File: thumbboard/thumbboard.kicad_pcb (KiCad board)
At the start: 2 copper layers, 79.7 x 37 mm, 6 parts, among them J1 Conn_01x05_MountingPin, SW1 SW_Push, SW2 SW_Push, SW3 SW_Push, SW4 SW_Push

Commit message: sdf
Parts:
- removed the REF** at (114.1, 89.2)
- added REF**: NPTH 0.5mm, panelization:NPTH 0.5mm, F.Cu at (137.5, 80.0)
- added REF**: NPTH 0.5mm, panelization:NPTH 0.5mm, F.Cu at (137.5, 79.0)
- added REF**: NPTH 0.5mm, panelization:NPTH 0.5mm, F.Cu at (137.5, 78.0)
- added REF**: NPTH 0.5mm, panelization:NPTH 0.5mm, F.Cu at (128.5, 92.0)
- added REF**: NPTH 0.5mm, panelization:NPTH 0.5mm, F.Cu at (128.5, 90.0)
- added REF**: NPTH 0.5mm, panelization:NPTH 0.5mm, F.Cu at (128.5, 91.0)
- moved SW4 8.06 mm to (169.0, 85.0), turned to -90 degrees
- moved J1 7.07 mm to (145.0, 78.9)
- moved SW1 7.07 mm to (145.0, 85.0)
- moved SW2 7.07 mm to (145.0, 105.5)
- moved SW3 2.24 mm to (121.0, 85.0), turned to 90 degrees
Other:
- board size 79.7 x 37 mm -> 63 x 37 mm

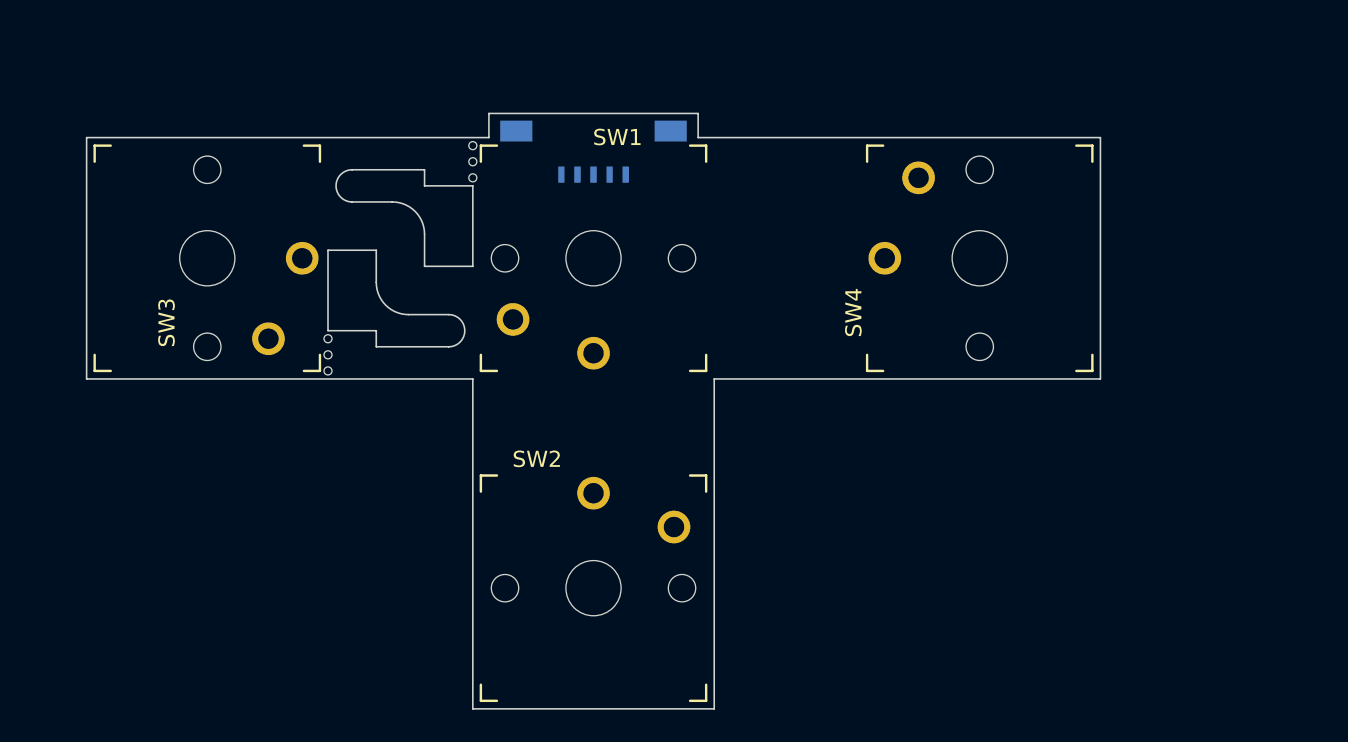
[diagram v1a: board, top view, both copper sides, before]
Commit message: small tweaks, incl thumbboard side springs (and fabrication frame)
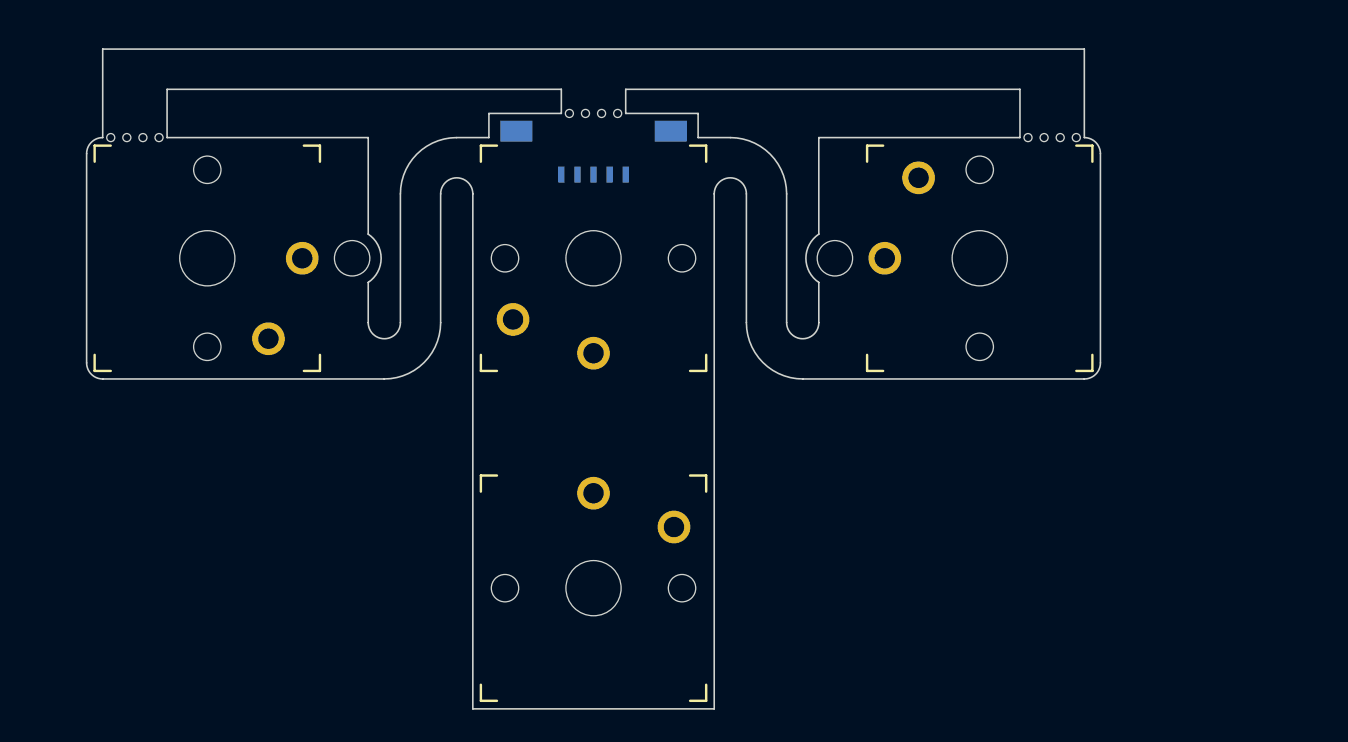
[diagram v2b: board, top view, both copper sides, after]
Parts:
- removed the REF** at (137.5, 80.0)
- removed the REF** at (137.5, 79.0)
- removed the REF** at (137.5, 78.0)
- removed the REF** at (128.5, 92.0)
- removed the REF** at (128.5, 90.0)
- removed the REF** at (128.5, 91.0)
- added REF**: NPTH 0.5mm, panelization:NPTH 0.5mm, F.Cu at (145.5, 76.0)
- added REF**: NPTH 0.5mm, panelization:NPTH 0.5mm, B.Cu at (175.0, 77.5)
- added REF**: NPTH 0.5mm, panelization:NPTH 0.5mm, B.Cu at (174.0, 77.5)
- added REF**: NPTH 0.5mm, panelization:NPTH 0.5mm, B.Cu at (173.0, 77.5)
- added REF**: NPTH 0.5mm, panelization:NPTH 0.5mm, B.Cu at (172.0, 77.5)
- added REF**: NPTH 2.2mm, panelization:NPTH 2.2mm, B.Cu at (160.0, 85.0)
- added REF**: NPTH 0.5mm, panelization:NPTH 0.5mm, F.Cu at (115.0, 77.5)
- added REF**: NPTH 0.5mm, panelization:NPTH 0.5mm, F.Cu at (144.5, 76.0)
- added REF**: NPTH 2.2mm, panelization:NPTH 2.2mm, F.Cu at (130.0, 85.0)
- added REF**: NPTH 0.5mm, panelization:NPTH 0.5mm, F.Cu at (146.5, 76.0)
- added REF**: NPTH 0.5mm, panelization:NPTH 0.5mm, F.Cu at (118.0, 77.5)
- added REF**: NPTH 0.5mm, panelization:NPTH 0.5mm, F.Cu at (116.0, 77.5)
- added REF**: NPTH 0.5mm, panelization:NPTH 0.5mm, F.Cu at (143.5, 76.0)
- added REF**: NPTH 0.5mm, panelization:NPTH 0.5mm, F.Cu at (117.0, 77.5)
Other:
- board size 63 x 37 mm -> 63 x 41 mm

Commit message: layout and cleanups (but J1 still in the wrong spot)
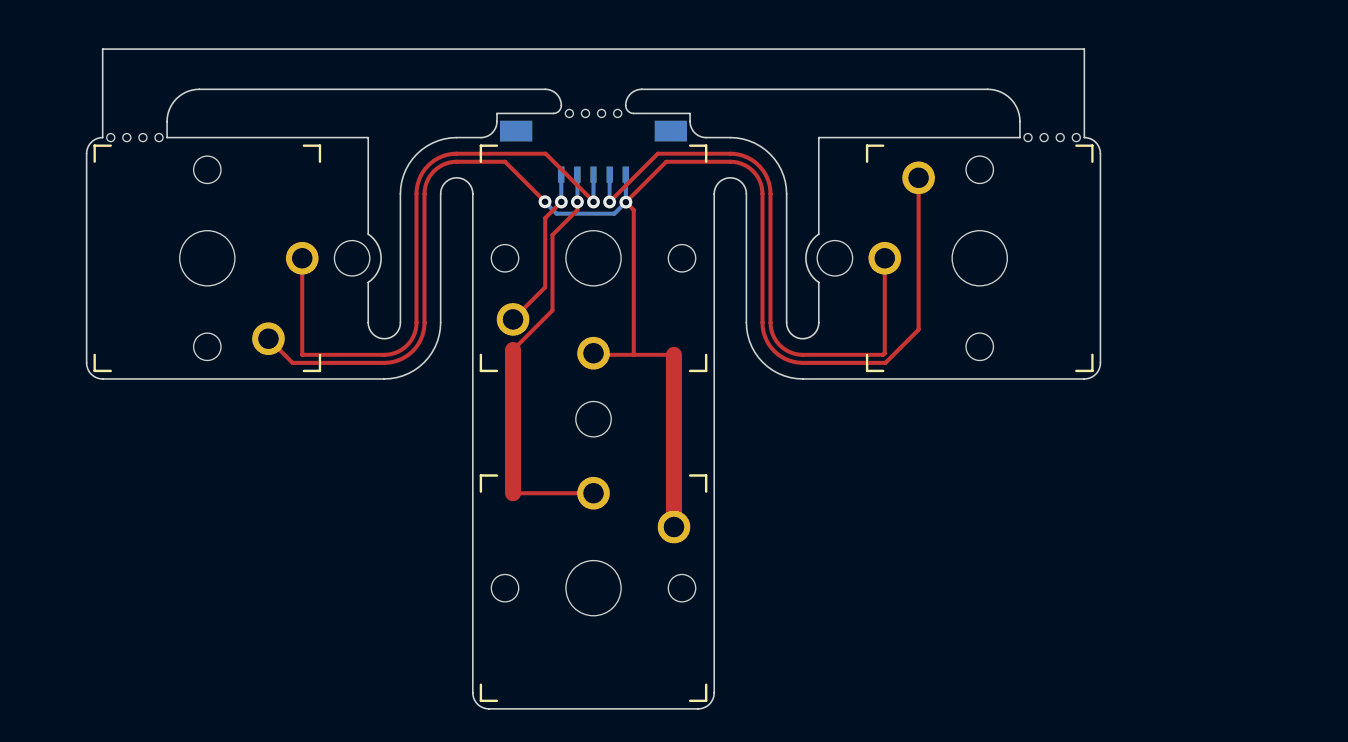
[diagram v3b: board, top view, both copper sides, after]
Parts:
- added REF**: NPTH 2.2mm, panelization:NPTH 2.2mm, F.Cu at (145.0, 95.0)
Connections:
- SW1 pad 1: ROW_A -> COL
- SW1 pad 2: COL -> ROW_A
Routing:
- net COL: track 0.00 -> 102.0 mm, vias 0 -> 2
- net ROW_C: track 0.00 -> 37.4 mm, vias 0 -> 1
- net ROW_D: track 0.00 -> 36.4 mm, vias 0 -> 1
- net ROW_B: track 0.00 -> 26.5 mm, vias 0 -> 1
- net ROW_A: track 0.00 -> 10.2 mm, vias 0 -> 1
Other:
- outline, holes or cut-outs redrawn

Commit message: more tweaks to thumbboard, incl changing pinout
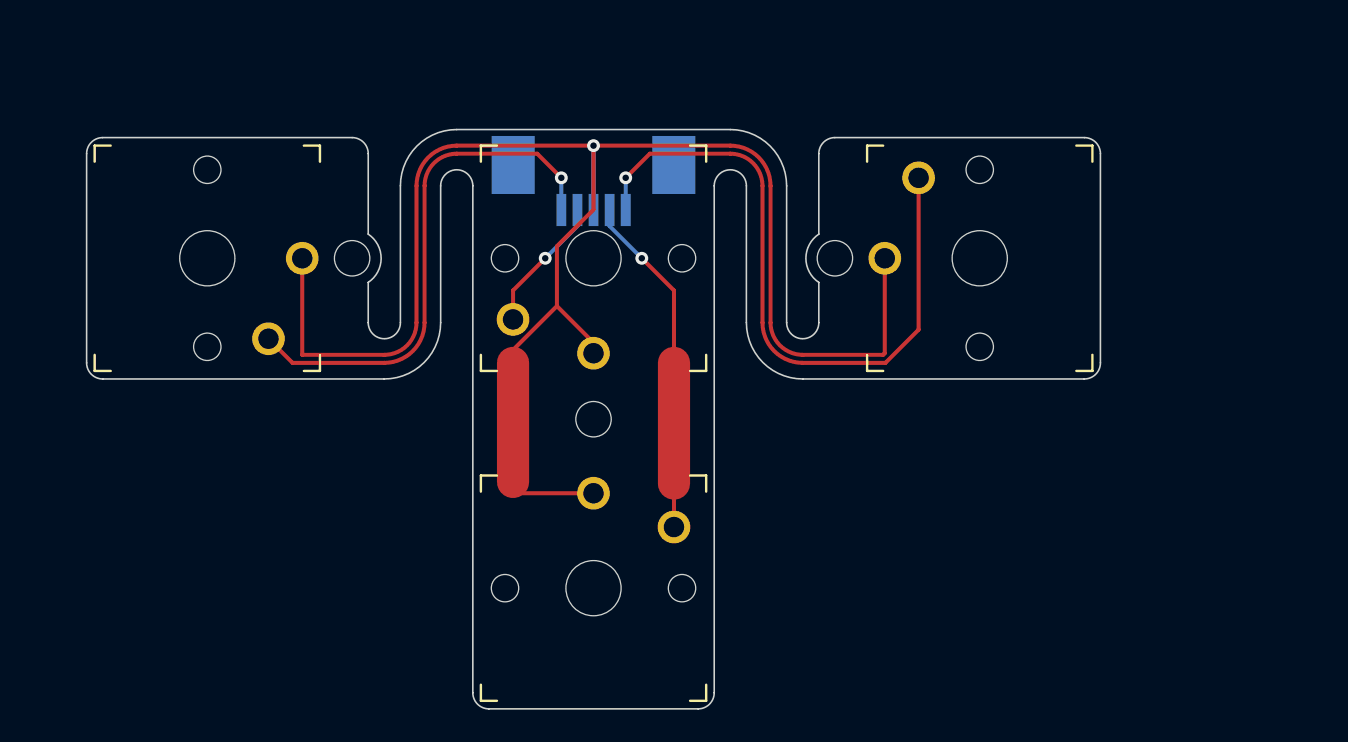
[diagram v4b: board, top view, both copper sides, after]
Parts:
- removed the REF** at (145.5, 76.0)
- removed the REF** at (117.0, 77.5)
- removed the REF** at (175.0, 77.5)
- removed the REF** at (174.0, 77.5)
- removed the REF** at (173.0, 77.5)
- removed the REF** at (172.0, 77.5)
- removed the REF** at (115.0, 77.5)
- removed the REF** at (144.5, 76.0)
- removed the REF** at (146.5, 76.0)
- removed the REF** at (118.0, 77.5)
- removed the REF** at (116.0, 77.5)
- removed the REF** at (143.5, 76.0)
- J1: footprint Connector_FFC-FPC:Molex_200528-0050_1x05-1MP_P1.00mm_Horizontal -> Connector_FFC-FPC:TE_84952-5_1x05-1MP_P1.0mm_Horizontal
- moved SW3 31.6 mm to (145.0, 105.5), turned to 180 degrees
- moved SW1 24.0 mm to (121.0, 85.0), turned to 90 degrees
- moved SW2 20.5 mm to (145.0, 85.0), turned to 0 degrees
- moved J1 1.31 mm to (145.0, 80.2)
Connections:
- J1 pad 3: ROW_C -> COL
- J1 pad 4: ROW_D -> ROW_C
- J1 pad 5: COL -> ROW_D
- SW2 pad 1: ROW_B -> COL
- SW2 pad 2: COL -> ROW_B
- SW3 pad 1: ROW_C -> COL
- SW3 pad 2: COL -> ROW_C
- SW4 pad 1: ROW_D -> COL
- SW4 pad 2: COL -> ROW_D
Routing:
- net ROW_A: track 10.2 -> 32.3 mm
- net ROW_B: track 26.5 -> 8.46 mm
- net ROW_C: track 37.4 -> 20.9 mm
- net ROW_D: track 36.4 -> 42.0 mm
- net COL: track 102.0 -> 104.6 mm, vias 2 -> 1
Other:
- board size 63 x 41 mm -> 63 x 36 mm
